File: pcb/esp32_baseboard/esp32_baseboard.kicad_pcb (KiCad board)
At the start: 2 copper layers, 185 x 120 mm, 84 parts, among them J1 24V_IN, J14 BUP_U, J15 FIBER, U1 STM32G030C8T6, U2 MP1584EN, U3 TMC1, U4 TMC2, U44 PC817, U45 PC817, U46 PC817, U47 PC817, U5 CH340C, U6 AMS1117-3.3, Y1 12MHz

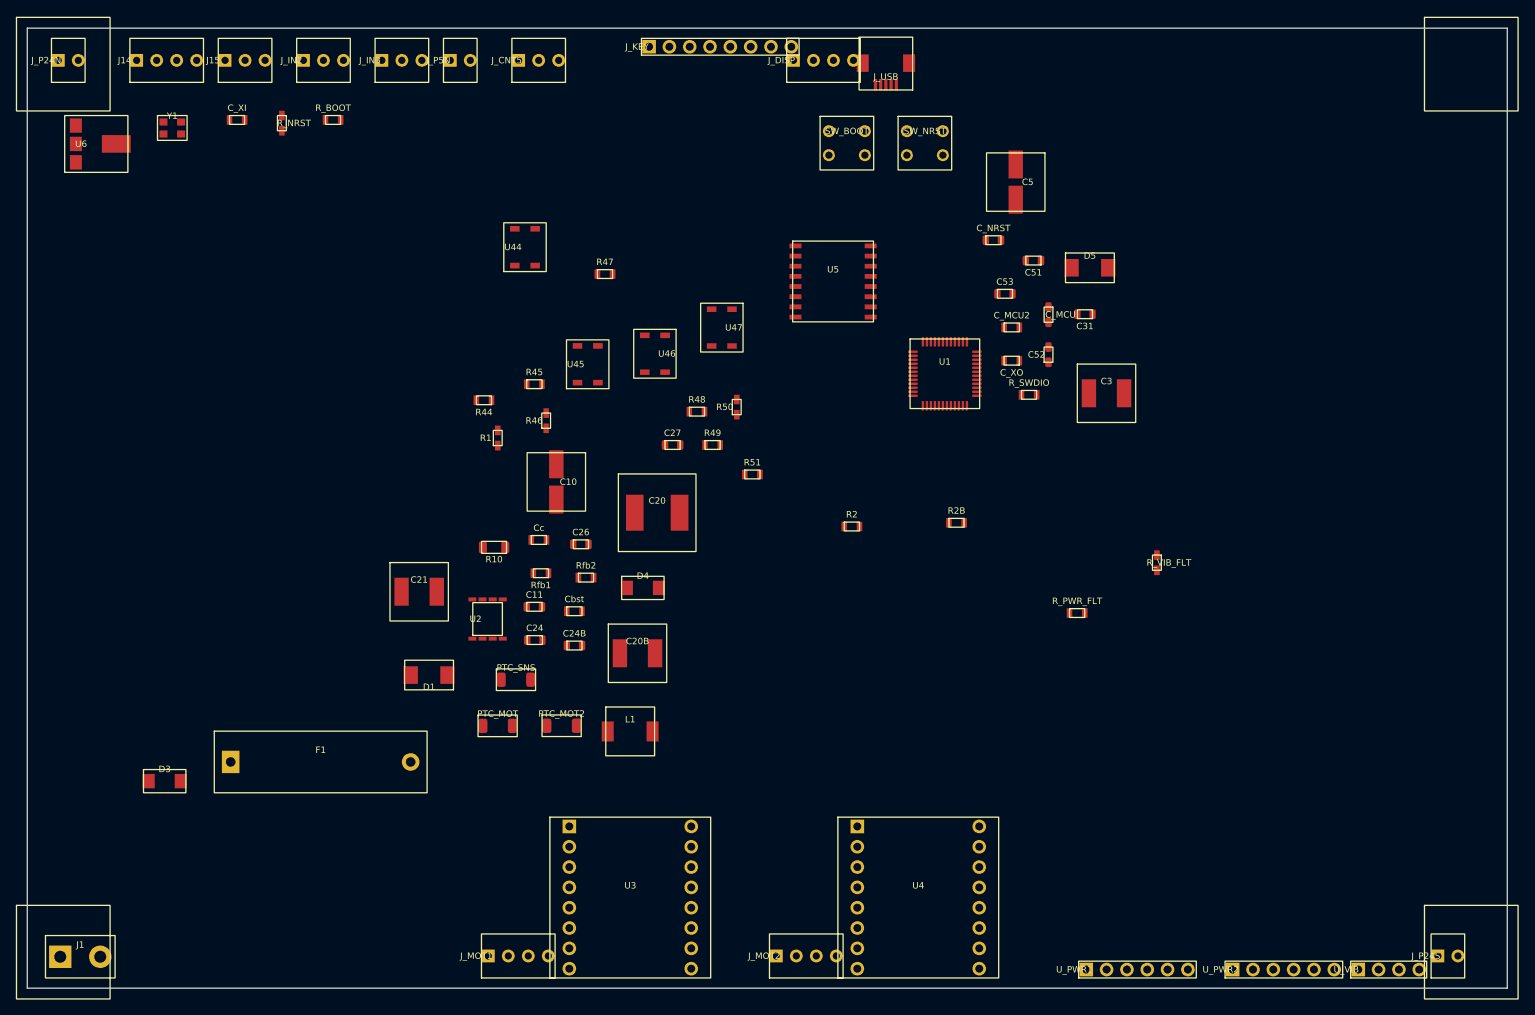
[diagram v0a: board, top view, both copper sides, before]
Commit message: chuẩn hóa layout mạch để phù hợp nhiều loại hộp
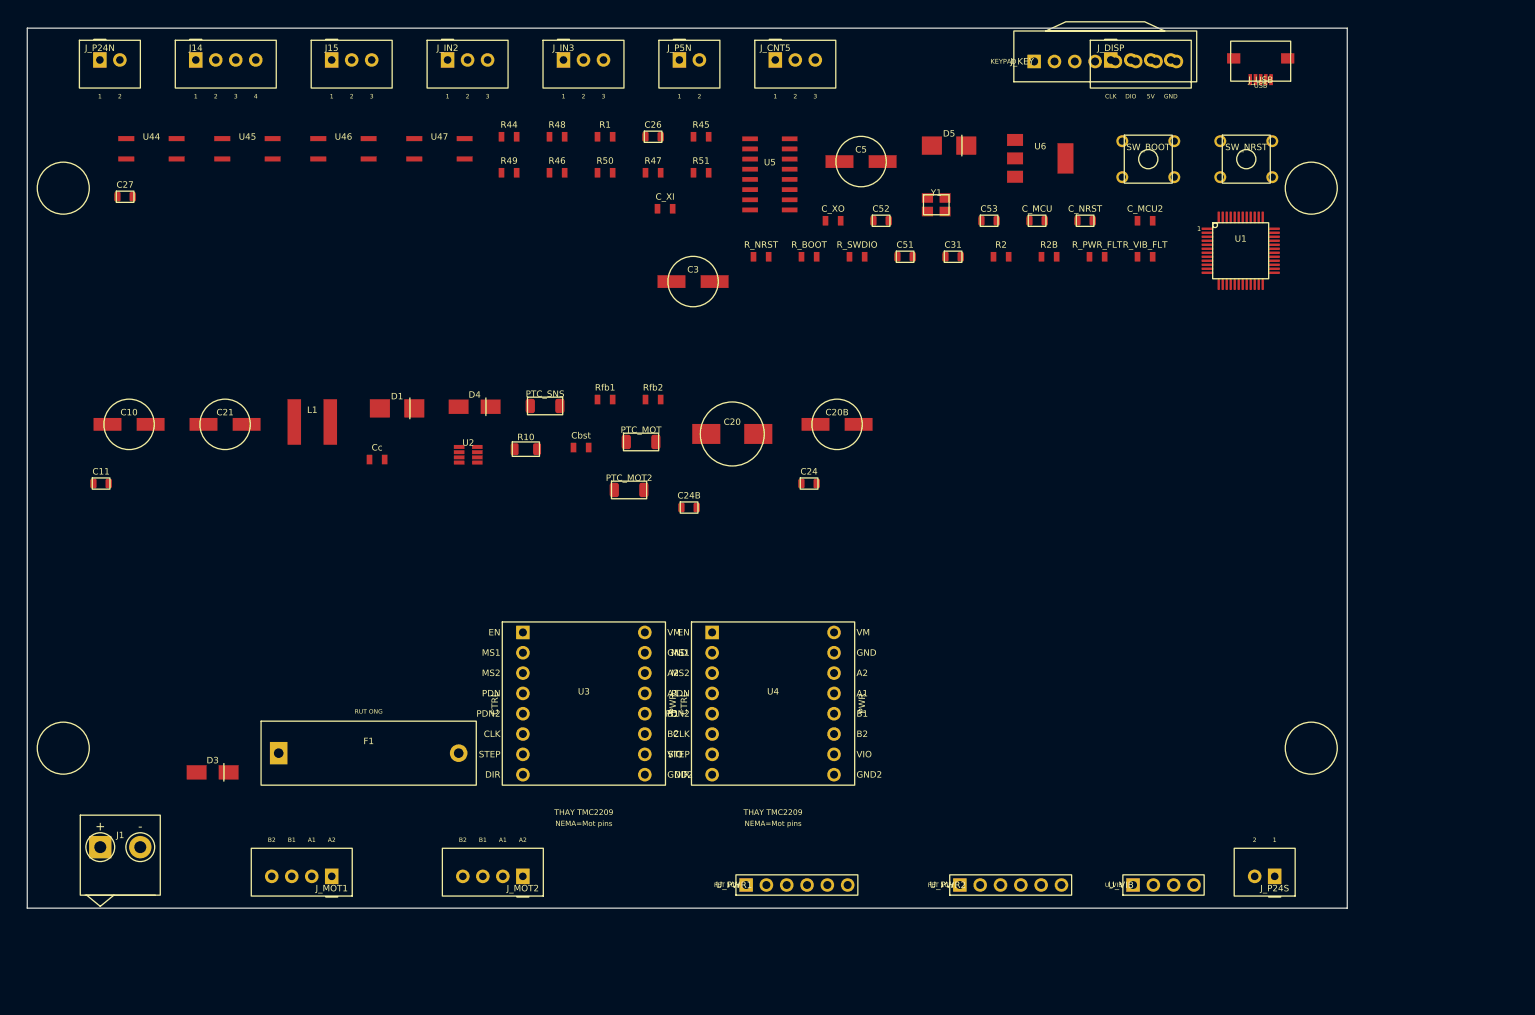
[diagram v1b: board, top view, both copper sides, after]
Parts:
- moved U6 118.4 mm to (176.6, 66.3), turned to 0 degrees
- moved Y1 96.0 mm to (163.6, 72.1)
- moved C27 75.1 mm to (62.2, 71.1)
- moved R_NRST 62.2 mm to (141.7, 78.6), turned to 0 degrees
- moved R_BOOT 61.9 mm to (147.7, 78.6)
- moved C11 56.3 mm to (59.2, 106.9)
- moved L1 55.5 mm to (85.6, 99.2)
- moved C_XI 54.6 mm to (129.7, 72.6)
- moved C10 53.9 mm to (62.7, 99.5), turned to 0 degrees
- moved C3 53.5 mm to (133.2, 81.7)
- moved C26 51.7 mm to (128.2, 63.6)
- moved U45 50.3 mm to (77.5, 65.1), turned to 0 degrees
- moved U44 48.3 mm to (65.5, 65.1), turned to 0 degrees
- moved J_KEY 48.2 mm to (175.9, 54.2)
- moved J_USB 46.9 mm to (204.2, 55.0)
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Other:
- board size 185 x 120 mm -> 165 x 110 mm
- board text added: "165x110 | L/R 8mm DIN/clip | box 180x130 / 200x150"
- board text added: "N: SNS/HMI/USB | S: J1 MOT1 MOT2 PWR1 PWR2 VIB P24 | TMC inland"
- board text removed: "185x120 DIN | field jacks N/S only | W/E=rail"
- board text removed: "N: SNS/HMI/USB | S: J1 MOT1 U3 MOT2 U4 PWR1 PWR2 VIB P24"

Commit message: update 3d view để khớp với PCB
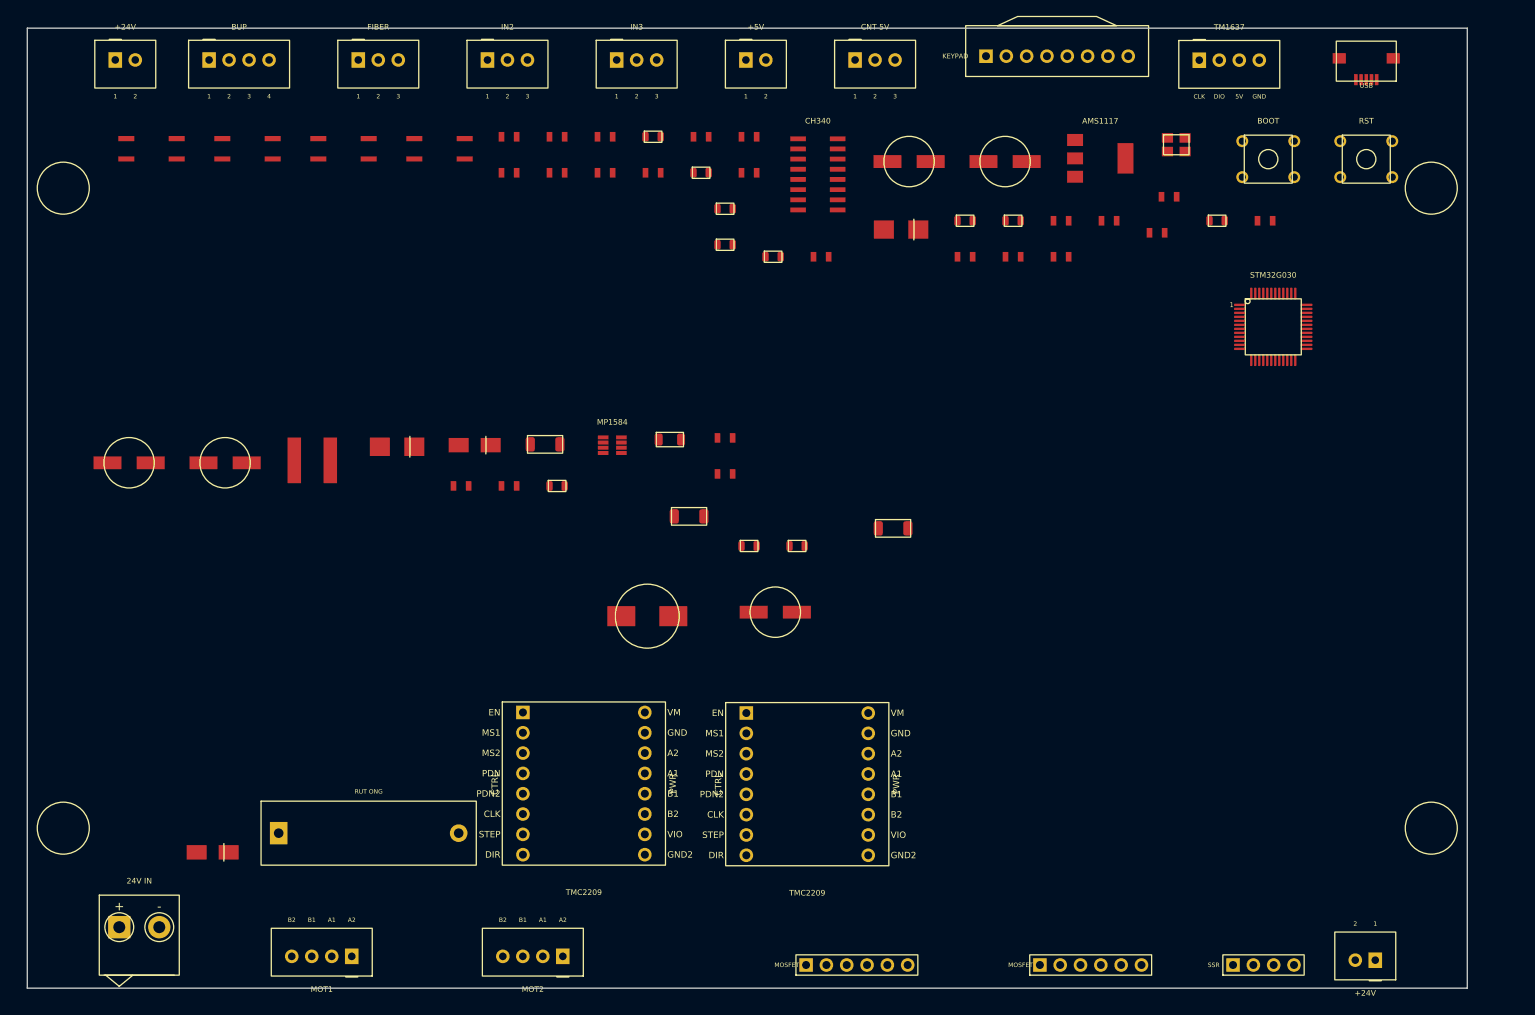
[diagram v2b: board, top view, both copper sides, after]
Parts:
- J_DISP: value TM1637_MOD -> TM1637
- J_KEY: value KEYPAD_EXT -> KEYPAD
- J_USB: value USB_MicroB -> USB
- U1: value STM32G030C8T6 -> STM32G030
- U3: value TMC1 -> TMC2209
- U4: value TMC2 -> TMC2209
- U_PWR1: value FET1 -> MOSFET
- U_PWR2: value FET2 -> MOSFET
- U_VIB: value VIB_SSR -> SSR
- moved C27 72.1 mm to (134.2, 68.1)
- moved R_BOOT 57.2 mm to (204.7, 74.1)
- moved C11 57.0 mm to (116.2, 107.2)
- moved R_NRST 43.7 mm to (185.2, 74.1)
- moved C_XO 42.1 mm to (192.7, 71.1)
- moved C3 41.8 mm to (172.2, 66.7)
- moved R_SWDIO 37.6 mm to (191.2, 75.6)
- moved PTC_MOT2 33.3 mm to (158.2, 112.5)
- moved Y1 30.9 mm to (193.6, 64.6)
- moved R49 30.3 mm to (140.2, 63.6)
- moved C20 25.1 mm to (127.5, 123.5)
- moved C20B 24.7 mm to (143.5, 123.0)
- moved C51 22.5 mm to (137.2, 77.1)
- moved C31 22.5 mm to (143.2, 78.6)
- moved R2 22.5 mm to (149.2, 78.6)
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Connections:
- J14 pad 4: (no net) -> unconnected-(J14-ENC_B-Pad4)
- J_USB pad 4: (no net) -> unconnected-(J_USB-P4-Pad4)
- U1 pad 1: (no net) -> unconnected-(U1-P1-Pad1)
- U1 pad 2: (no net) -> unconnected-(U1-P2-Pad2)
- U1 pad 3: (no net) -> unconnected-(U1-P3-Pad3)
- U1 pad 30: (no net) -> unconnected-(U1-P30-Pad30)
- U1 pad 31: (no net) -> unconnected-(U1-P31-Pad31)
- U1 pad 37: (no net) -> unconnected-(U1-P37-Pad37)
- U1 pad 38: (no net) -> unconnected-(U1-P38-Pad38)
- U1 pad 40: (no net) -> unconnected-(U1-P40-Pad40)
- U1 pad 41: (no net) -> unconnected-(U1-P41-Pad41)
- U1 pad 42: (no net) -> unconnected-(U1-P42-Pad42)
- U1 pad 8: (no net) -> unconnected-(U1-P8-Pad8)
- U1 pad 9: (no net) -> unconnected-(U1-P9-Pad9)
- U2 pad 7: (no net) -> unconnected-(U2-P7-Pad7)
- U3 pad 2: (no net) -> unconnected-(U3-MS1-Pad2)
- U3 pad 3: (no net) -> unconnected-(U3-MS2-Pad3)
- U3 pad 4: (no net) -> unconnected-(U3-PDN-Pad4)
- U3 pad 5: (no net) -> unconnected-(U3-PDN2-Pad5)
- U3 pad 6: (no net) -> unconnected-(U3-CLK-Pad6)
- U4 pad 2: (no net) -> unconnected-(U4-MS1-Pad2)
- U4 pad 3: (no net) -> unconnected-(U4-MS2-Pad3)
- U4 pad 4: (no net) -> unconnected-(U4-PDN-Pad4)
- U4 pad 5: (no net) -> unconnected-(U4-PDN2-Pad5)
- U4 pad 6: (no net) -> unconnected-(U4-CLK-Pad6)
- U5 pad 10: (no net) -> unconnected-(U5-P10-Pad10)
- U5 pad 11: (no net) -> unconnected-(U5-P11-Pad11)
- U5 pad 12: (no net) -> unconnected-(U5-P12-Pad12)
- U5 pad 13: (no net) -> unconnected-(U5-P13-Pad13)
- U5 pad 14: (no net) -> unconnected-(U5-P14-Pad14)
- U5 pad 15: (no net) -> unconnected-(U5-P15-Pad15)
- U5 pad 9: (no net) -> unconnected-(U5-P9-Pad9)
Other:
- board size 165 x 110 mm -> 180 x 120 mm
- board text added: "180x120 | L/R 8mm DIN/clip | box 180x130 / 200x150"
- board text removed: "165x110 | L/R 8mm DIN/clip | box 180x130 / 200x150"
